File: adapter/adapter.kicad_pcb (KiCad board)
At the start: 2 copper layers, 43.5 x 38.6 mm, 22 parts, among them J2 Conn_01x06_Female, SW1 RotaryEncoder_Switch

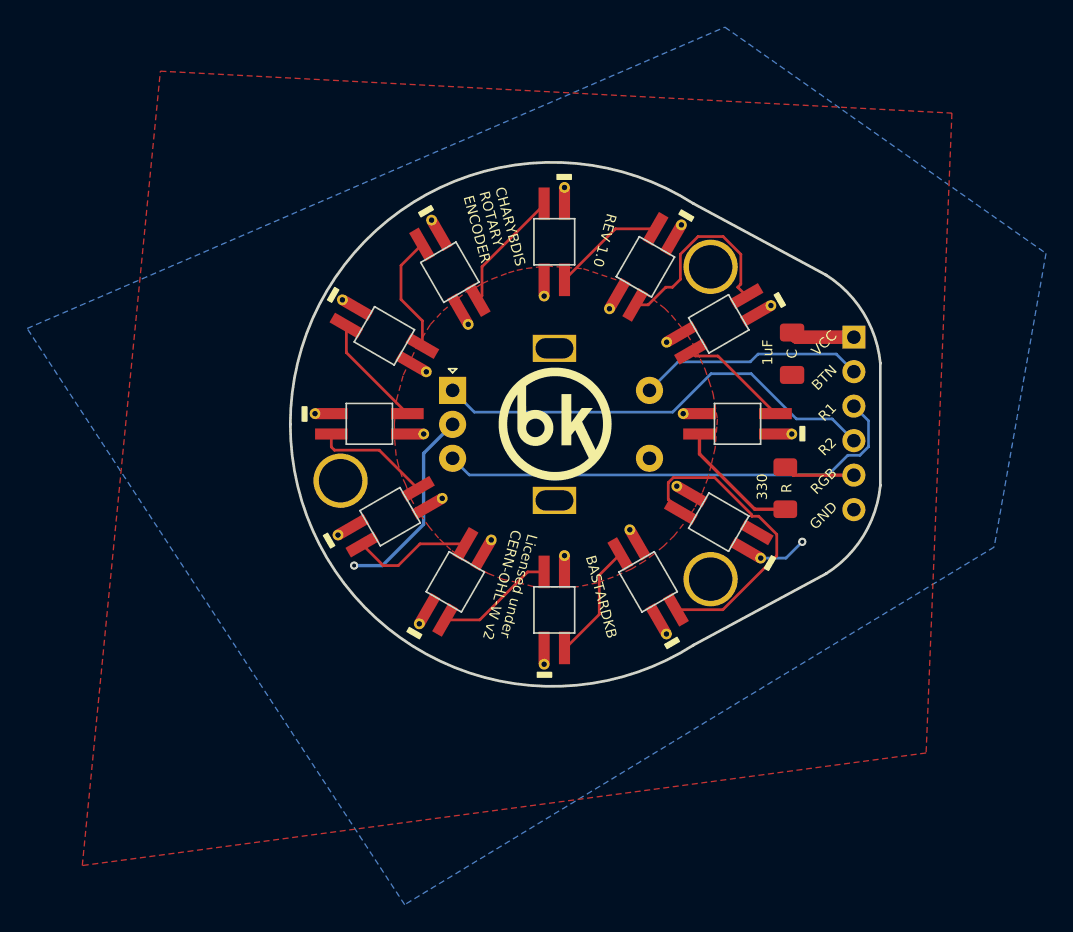
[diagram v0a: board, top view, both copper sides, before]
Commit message: complete reroute
- routing changed to fix din/dout paths
- added dout header
- renamed rgb header to din
- moved SMT components to bottom side
- changed silkscreen to rev 1.1
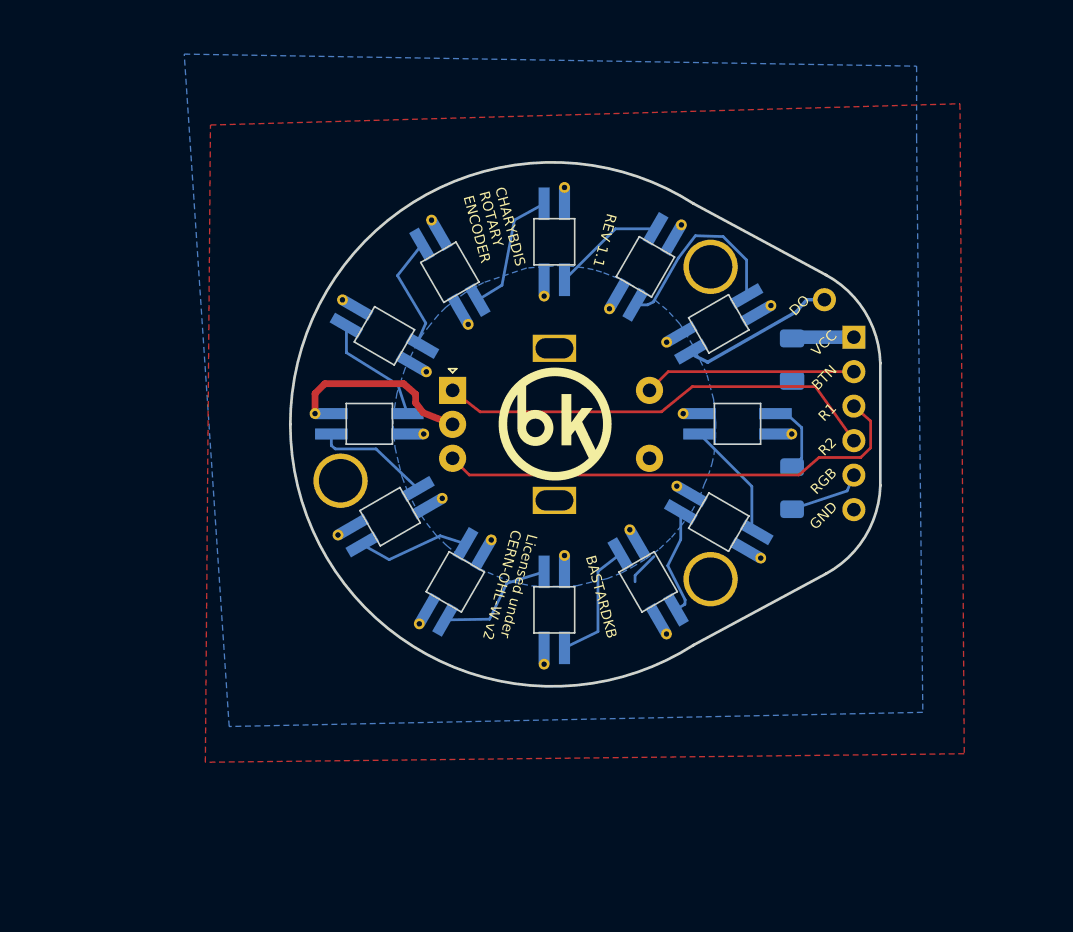
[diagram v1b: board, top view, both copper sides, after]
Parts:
- removed D1, D10, D11, D12, D2, D3, D4, D5, D6, D7, D8, D9: SK6812MINI, Library:YS-SK6812MINI-E
- added ?: , , F.Cu at (72.4, 34.4)
- added REF**: diy SK6812MINI-E, Library:diy SK6812MINI-E, B.Cu at (45.2, 55.2)
- added REF**: diy SK6812MINI-E, Library:diy SK6812MINI-E, B.Cu at (40.4, 50.4)
- added REF**: diy SK6812MINI-E, Library:diy SK6812MINI-E, B.Cu at (64.6, 50.8)
- added REF**: diy SK6812MINI-E, Library:diy SK6812MINI-E, B.Cu at (40.0, 37.1)
- added REF**: diy SK6812MINI-E, Library:diy SK6812MINI-E, B.Cu at (59.4, 55.2)
- added REF**: diy SK6812MINI-E, Library:diy SK6812MINI-E, B.Cu at (52.5, 30.2)
- added REF**: diy SK6812MINI-E, Library:diy SK6812MINI-E, B.Cu at (44.8, 32.4)
- added REF**: diy SK6812MINI-E, Library:diy SK6812MINI-E, B.Cu at (38.9, 43.6)
- added REF**: diy SK6812MINI-E, Library:diy SK6812MINI-E, B.Cu at (66.0, 43.6)
- added REF**: diy SK6812MINI-E, Library:diy SK6812MINI-E, B.Cu at (59.2, 32.0)
- added REF**: diy SK6812MINI-E, Library:diy SK6812MINI-E, B.Cu at (52.5, 57.3)
- added REF**: diy SK6812MINI-E, Library:diy SK6812MINI-E, B.Cu at (64.6, 36.2)
- C, R: moved to B.Cu
- moved R 0.50 mm to (70.0, 48.3)
- moved C 0.44 mm to (70.0, 38.8)
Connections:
- J2 pad 5: rgb -> DIN
- R pad 1: Net-(D1-Pad3) -> DIN
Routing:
- net Net-(D11-Pad3): track 23.1 -> 0.00 mm
- net Net-(D3-Pad1): track 14.9 -> 0.00 mm
- net Net-(D11-D12): track 0.00 -> 14.3 mm
- net DO: track 0.00 -> 11.5 mm
- net Net-(D9-D10): track 0.00 -> 9.48 mm
- net Net-(D1-Pad3): track 9.48 -> 0.00 mm
- net Net-(D3-D4): track 0.00 -> 9.26 mm
- net Net-(D2-Pad1): track 9.12 -> 0.00 mm
- net Net-(D4-D5): track 0.00 -> 9.08 mm
- net Net-(D1-D2): track 0.00 -> 8.99 mm
- net Net-(D8-D9): track 0.00 -> 8.95 mm
- net Net-(D12-Pad1): track 8.91 -> 0.00 mm
- net Net-(D4-Pad1): track 8.78 -> 0.00 mm
- net Net-(D7-Pad1): track 8.75 -> 0.00 mm
- net Net-(D7-D8): track 0.00 -> 8.70 mm
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- added copper zone on B.Cu, net Gnd
- removed copper zone on F.Cu, net Gnd
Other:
- board text added: "DO"
- board text added: "REV 1.1"
- board text removed: "REV 1.0"

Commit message: fixing drc flags
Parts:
- moved REF** 0.17 mm to (66.2, 43.6)
- moved REF** 0.09 mm to (40.0, 37.1)
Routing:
- net (no net): track 2.43 -> 0.00 mm
- net Net-(DIN-D1): track 5.54 -> 6.07 mm
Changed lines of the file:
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@@
-    (pad "6" thru_hole oval locked (at 0 6.28) (size 1.7 1.7) (drill 1) (layers *.Cu *.Mask)
-      (net 2 "Gnd") (pinfunction "Pin_6") (pintype "passive"))
     (pad "6" thru_hole oval locked (at 0 6.28) (size 1.7 1.7) (drill 1) (layers *.Cu *.Mask)
       (net 2 "Gnd") (pinfunction "Pin_6") (pintype "passive"))
@@
   )
   (footprint "Library:diy SK6812MINI-E" (layer "B.Cu")
-    (at 65.98 43.56 180)
+    (at 66.15 43.56 180)
     (attr through_hole)
     (fp_text reference "REF**" (at 0 -2.8) (layer "B.SilkS") hide
@@
   )
   (footprint "Library:diy SK6812MINI-E" (layer "B.Cu")
-    (at 39.98 37.08 -30)
+    (at 40.046 37.148 -30)
     (attr through_hole)
     (fp_text reference "REF**" (at 0 -2.8 150) (layer "B.SilkS") hide
@@
     (effects (font (size 0.75 0.75) (thickness 0.1)))
   )
-  (segment (start 58.438 54.723558) (end 59.82434 53.337218) (width 0.2032) (layer "B.Cu") (net 0))
-  (segment (start 58.438 55.193) (end 58.438 54.723558) (width 0.2032) (layer "B.Cu") (net 0))
-  (segment (start 70 36.8375) (end 70.3425 37.18) (width 0.2032) (layer "B.Cu") (net 1))
   (segment (start 70.3425 37.18) (end 74.55 37.18) (width 1) (layer "B.Cu") (net 1))
   (segment (start 34.87 42.81) (end 34.87 41.33) (width 0.5) (layer "F.Cu") (net 2))
@@
   (segment (start 71.080744 34.42) (end 72.381 34.42) (width 0.25) (layer "B.Cu") (net 7))
   (segment (start 62.550129 38.249519) (end 62.865476 38.564866) (width 0.2032) (layer "B.Cu") (net 7))
-  (segment (start 70.708 43.839) (end 70.708 46.086) (width 0.2032) (layer "B.Cu") (net 8))
-  (segment (start 70.708 46.086) (end 70 46.75) (width 0.2032) (layer "B.Cu") (net 8))
-  (segment (start 69.57 42.81) (end 70.708 43.839) (width 0.2032) (layer "B.Cu") (net 8))
+  (segment (start 69.57 42.81) (end 71.085 43.86) (width 0.2032) (layer "B.Cu") (net 8))
+  (segment (start 71.085 43.86) (end 71.085 45.944) (width 0.2032) (layer "B.Cu") (net 8))
+  (segment (start 71.085 45.944) (end 70 46.75) (width 0.2032) (layer "B.Cu") (net 8))
   (segment (start 68.78 42.81) (end 69.57 42.81) (width 0.2032) (layer "B.Cu") (net 8))
   (segment (start 67.038071 51.188681) (end 67.038071 48.168071) (width 0.2032) (layer "B.Cu") (net 9))
@@
   (segment (start 41.67 42.81) (end 40.97 40.678) (width 0.2032) (layer "B.Cu") (net 15))
   (segment (start 40.97 40.678) (end 37.180129 38.320129) (width 0.2032) (layer "B.Cu") (net 15))
+  (segment (start 42.845871 37.898481) (end 42.779871 37.830481) (width 0.2032) (layer "B.Cu") (net 16))
   (segment (start 42.750481 30.350129) (end 40.943 32.643) (width 0.2032) (layer "B.Cu") (net 16))
-  (segment (start 42.435134 37.485744) (end 42.779871 37.830481) (width 0.2032) (layer "B.Cu") (net 16))
+  (segment (start 43.027 36.143) (end 42.845871 37.898481) (width 0.2032) (layer "B.Cu") (net 16))
   (segment (start 40.943 32.643) (end 43.027 36.143) (width 0.2032) (layer "B.Cu") (net 16))
-  (segment (start 43.027 36.143) (end 42.435134 37.485744) (width 0.2032) (layer "B.Cu") (net 16))
   (segment (start 51.74 27.355) (end 49.551 28.557) (width 0.2032) (layer "B.Cu") (net 17))
   (segment (start 48.638 33.351) (end 46.849519 34.449871) (width 0.2032) (layer "B.Cu") (net 17))
@@
   (segment (start 59.950481 29.200129) (end 56.994871 29.200129) (width 0.2032) (layer "B.Cu") (net 18))
   (segment (start 56.994871 29.200129) (end 53.24 32.955) (width 0.2032) (layer "B.Cu") (net 18))
-  (segment (start 66.649871 34.146129) (end 66.651 34.145) (width 0.2032) (layer "B.Cu") (net 19))
-  (segment (start 66.649871 34.150481) (end 66.649871 34.146129) (width 0.2032) (layer "B.Cu") (net 19))
   (segment (start 62.879 29.71) (end 61.626 31.353) (width 0.2032) (layer "B.Cu") (net 19))
   (segment (start 59.359129 34.799871) (end 58.449519 34.799871) (width 0.2032) (layer "B.Cu") (net 19))

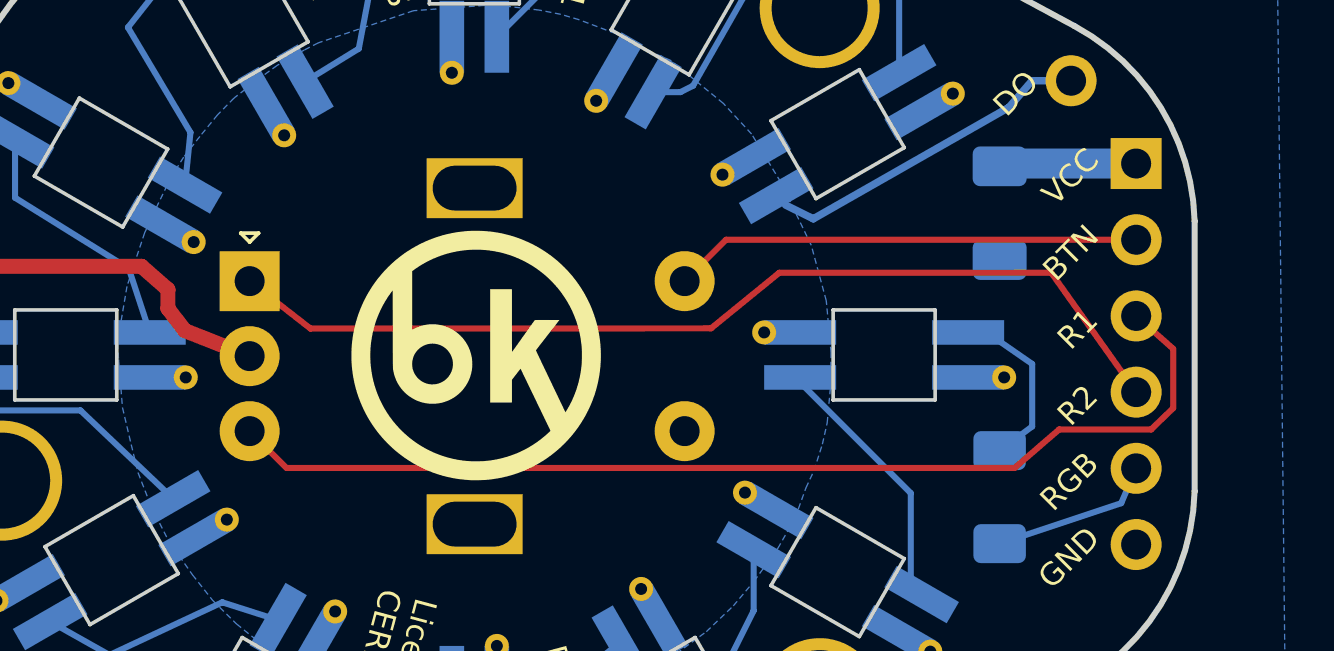
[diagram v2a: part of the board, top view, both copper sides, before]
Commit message: change vcc zone clearance
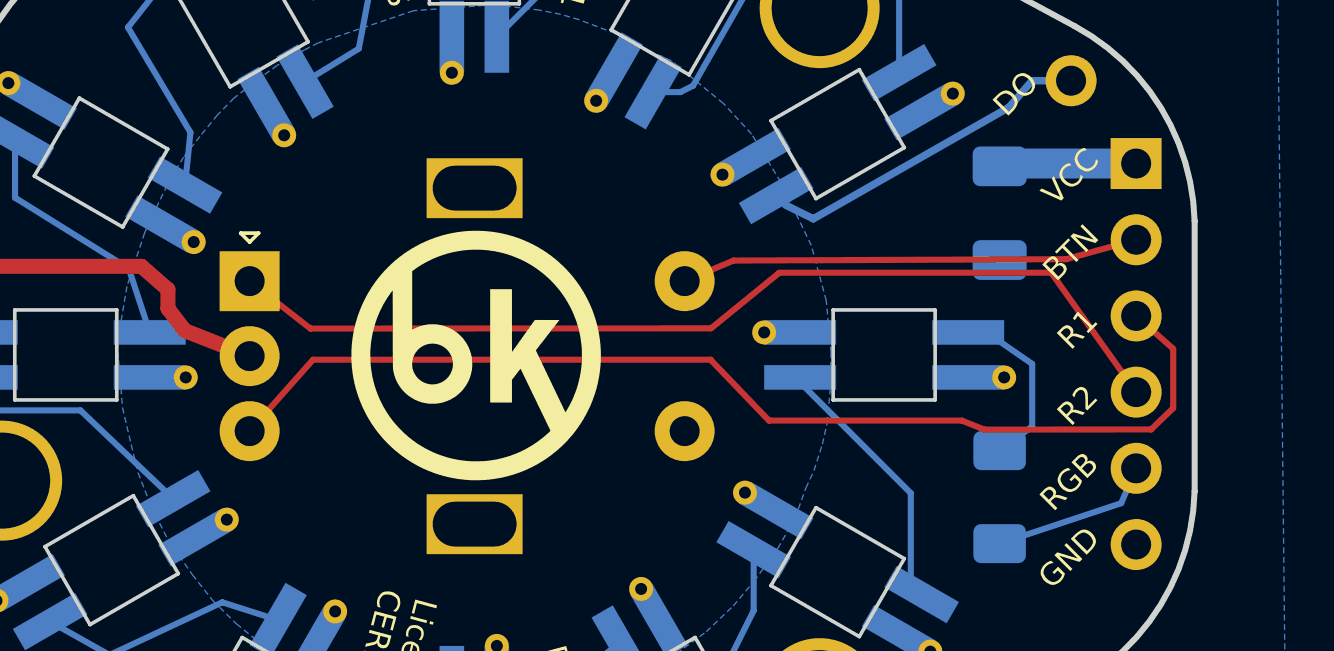
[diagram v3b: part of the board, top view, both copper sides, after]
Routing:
- net r1: track 35.7 -> 36.7 mm
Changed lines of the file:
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@@
   (segment (start 42.276 42.014) (end 42.839 42.749) (width 0.5) (layer "F.Cu") (net 2))
   (segment (start 34.87 41.33) (end 35.594 40.606) (width 0.5) (layer "F.Cu") (net 2))
-  (segment (start 59.5 41.1) (end 60.88 39.72) (width 0.2032) (layer "F.Cu") (net 3))
-  (segment (start 60.88 39.72) (end 74.55 39.72) (width 0.2032) (layer "F.Cu") (net 3))
-  (segment (start 70.497209 47.328111) (end 71.983 46.044) (width 0.2032) (layer "F.Cu") (net 4))
-  (segment (start 45 46.1) (end 46.228111 47.328111) (width 0.2032) (layer "F.Cu") (net 4))
-  (segment (start 75.785 43.356) (end 74.55 42.26) (width 0.2032) (layer "F.Cu") (net 4))
+  (segment (start 72.218 40.369) (end 74.55 39.72) (width 0.2032) (layer "F.Cu") (net 3))
+  (segment (start 59.5 41.1) (end 61.131 40.414) (width 0.2032) (layer "F.Cu") (net 3))
+  (segment (start 61.131 40.414) (end 72.218 40.369) (width 0.2032) (layer "F.Cu") (net 3))
+  (segment (start 47.112 43.719) (end 60.364 43.719) (width 0.2032) (layer "F.Cu") (net 4))
+  (segment (start 68.74 45.749) (end 69.489 46.048) (width 0.2032) (layer "F.Cu") (net 4))
   (segment (start 75.785 45.332) (end 75.785 43.356) (width 0.2032) (layer "F.Cu") (net 4))
   (segment (start 75.05 46.044) (end 75.785 45.332) (width 0.2032) (layer "F.Cu") (net 4))
-  (segment (start 46.228111 47.328111) (end 70.497209 47.328111) (width 0.2032) (layer "F.Cu") (net 4))
-  (segment (start 71.983 46.044) (end 75.05 46.044) (width 0.2032) (layer "F.Cu") (net 4))
+  (segment (start 69.489 46.048) (end 75.05 46.044) (width 0.2032) (layer "F.Cu") (net 4))
+  (segment (start 62.311 45.749) (end 68.74 45.749) (width 0.2032) (layer "F.Cu") (net 4))
+  (segment (start 45 46.1) (end 47.112 43.719) (width 0.2032) (layer "F.Cu") (net 4))
+  (segment (start 60.364 43.719) (end 62.311 45.749) (width 0.2032) (layer "F.Cu") (net 4))
+  (segment (start 75.785 43.356) (end 74.55 42.26) (width 0.2032) (layer "F.Cu") (net 4))
   (segment (start 47.026 42.681) (end 60.38 42.674) (width 0.2032) (layer "F.Cu") (net 5))
   (segment (start 62.654 40.821) (end 71.72 40.819) (width 0.2032) (layer "F.Cu") (net 5))
@@
   (segment (start 41.67 42.81) (end 40.97 40.678) (width 0.2032) (layer "B.Cu") (net 15))
   (segment (start 40.97 40.678) (end 37.180129 38.320129) (width 0.2032) (layer "B.Cu") (net 15))
-  (segment (start 42.845871 37.898481) (end 42.779871 37.830481) (width 0.2032) (layer "B.Cu") (net 16))
   (segment (start 42.750481 30.350129) (end 40.943 32.643) (width 0.2032) (layer "B.Cu") (net 16))
   (segment (start 43.027 36.143) (end 42.845871 37.898481) (width 0.2032) (layer "B.Cu") (net 16))
@@
   (segment (start 61.626 31.353) (end 59.782 34.585) (width 0.2032) (layer "B.Cu") (net 19))
   (zone (net 1) (net_name "Vcc") (layer "F.Cu") (hatch edge 0.508)
-    (connect_pads (clearance 0.254))
+    (connect_pads (clearance 0.58))
     (min_thickness 0.254) (filled_areas_thickness no)
     (fill yes (thermal_gap 0.508) (thermal_bridge_width 0.508) (island_removal_mode 1) (island_area_min 0))
